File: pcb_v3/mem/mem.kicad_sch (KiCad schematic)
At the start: 27 parts, among them J1 bus mem, J2 bus mem, J3 cartridge, U1 CY62256-70PC, U2 CY62256-70PC, U3 74LS283, U4 74LS00, U5 74LS32, U7 74LS138

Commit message: avançando no layot v3
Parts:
- added J4: addr in, edge_connector:conector 02x08, symbol Connector_Generic:Conn_02x08_Odd_Even
- added RN1, RN2: 10K, Resistor_THT:R_Array_SIP9, symbol Device:R_Network08
- J1, J2: footprint Connector_PinHeader_2.54mm:PinHeader_2x08_P2.54mm_Vertical -> edge_connector:conector 02x08
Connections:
- net +5V: now also RN1.1 (common), RN2.1 (common)
- net addr_{0}: now also J4.2 (Pin_2), RN1.9 (R8)
- net addr_{10}: now also J4.12 (Pin_12), RN2.7 (R6)
- net addr_{11}: now also J4.11 (Pin_11), RN2.6 (R5)
- net addr_{12}: now also J4.14 (Pin_14), RN2.5 (R4)
- net addr_{13}: now also J4.13 (Pin_13), RN2.4 (R3)
- net addr_{14}: now also J4.16 (Pin_16), RN2.3 (R2)
- net addr_{15}: now also J4.15 (Pin_15), RN2.2 (R1)
- net addr_{1}: now also J4.1 (Pin_1), RN1.8 (R7)
- net addr_{2}: now also J4.4 (Pin_4), RN1.7 (R6)
- net addr_{3}: now also J4.3 (Pin_3), RN1.6 (R5)
- net addr_{4}: now also J4.6 (Pin_6), RN1.5 (R4)
- net addr_{5}: now also J4.5 (Pin_5), RN1.4 (R3)
- net addr_{6}: now also J4.8 (Pin_8), RN1.3 (R2)
- net addr_{7}: now also J4.7 (Pin_7), RN1.2 (R1)
- net addr_{8}: now also J4.10 (Pin_10), RN2.9 (R8)
- net addr_{9}: now also J4.9 (Pin_9), RN2.8 (R7)
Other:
- moved on the sheet: J2

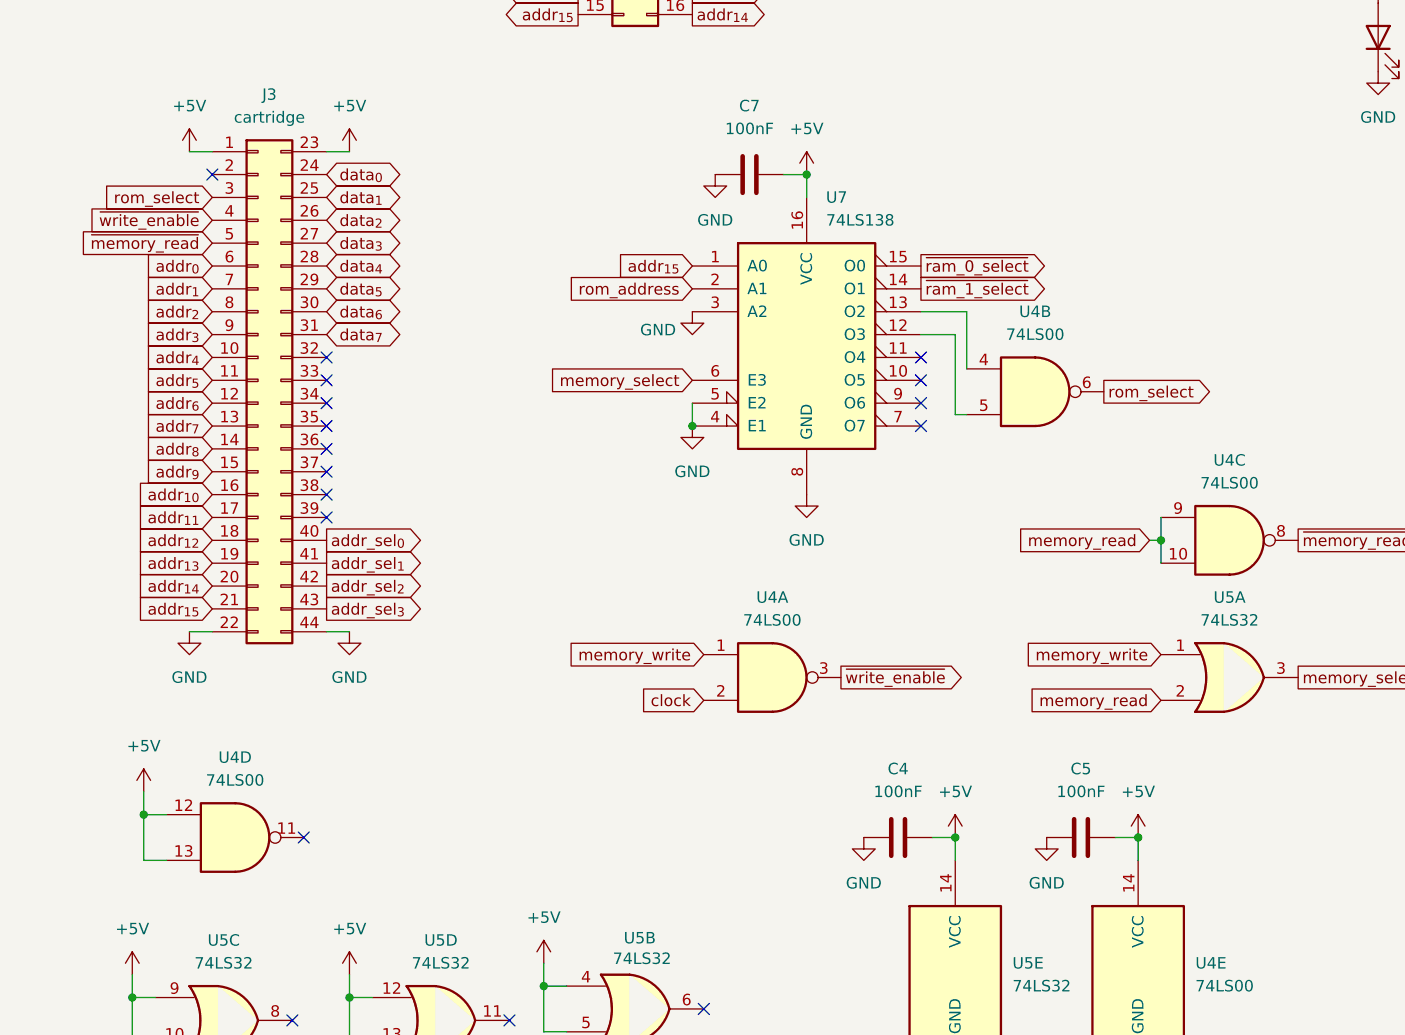
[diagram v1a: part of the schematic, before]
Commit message: seleção de chip de rom feita pela placa de memória; isso reduz um chip no cartucho
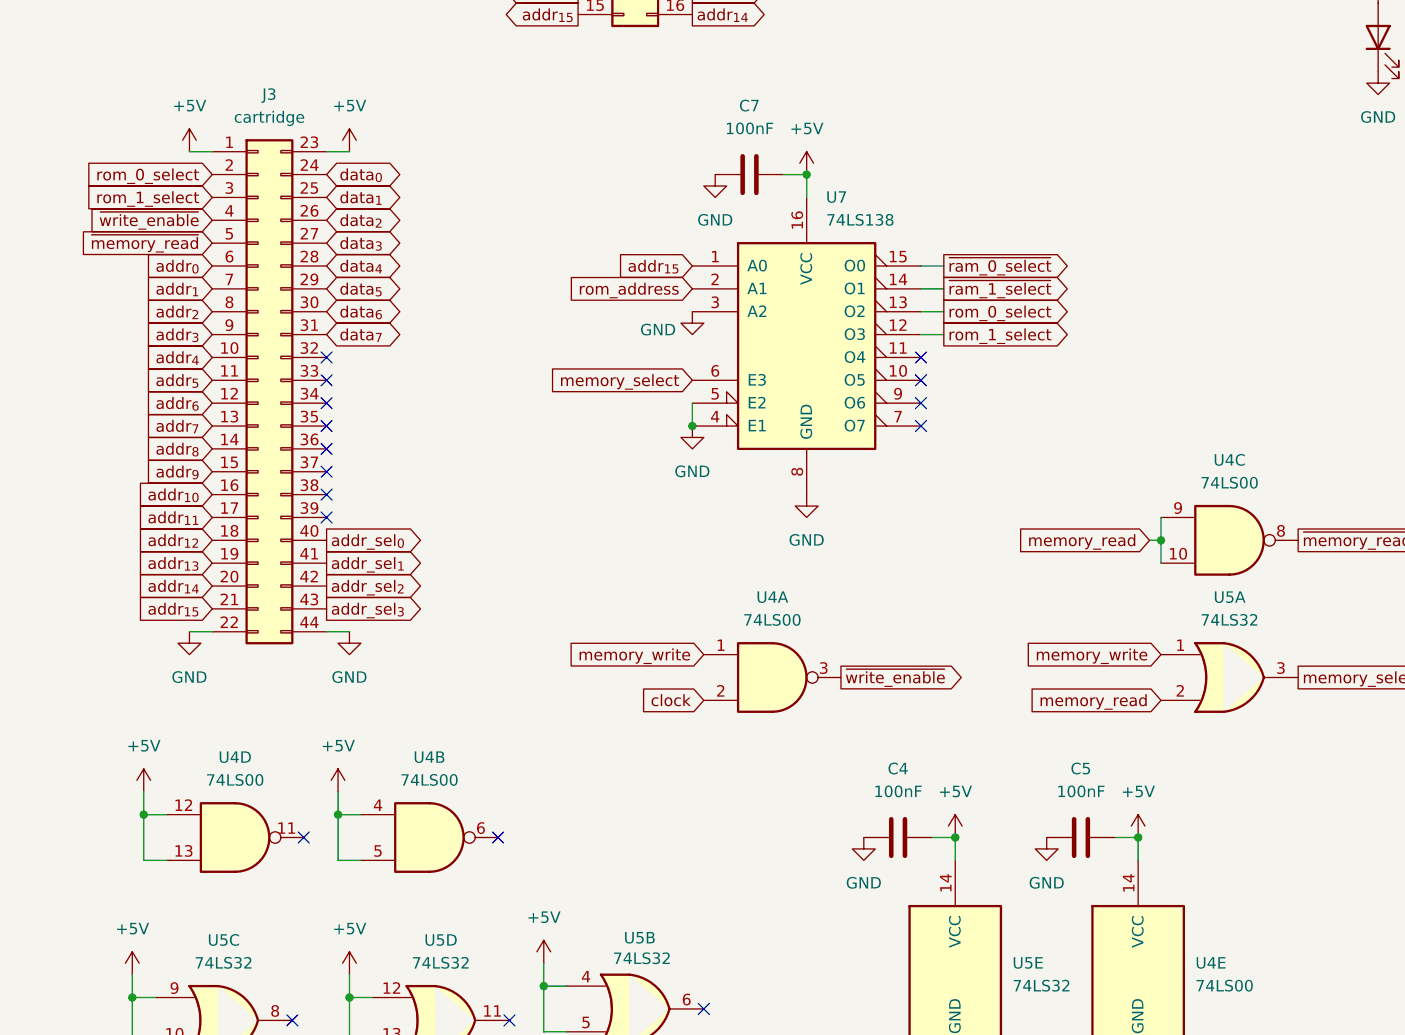
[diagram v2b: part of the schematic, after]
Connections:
- net +5V: now also U4.4, U4.5
- net rom_select: no longer J3.3 (Pin_3), U4.6
- net rom_0_select: now reaches U7.13 (O2)
- net rom_0_select: now also J3.2 (Pin_2); no longer U4.4
- net rom_1_select: now reaches U7.12 (O3)
- net rom_1_select: now also J3.3 (Pin_3); no longer U4.5
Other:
- moved on the sheet: U4B
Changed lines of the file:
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@@
 	)
 	(junction
+		(at 44.45 156.21)
+		(diameter 0)
+		(color 0 0 0 0)
+	)
+	(junction
 		(at 21.59 176.53)
 		(diameter 0)
@@
 	)
 	(no_connect
-		(at 30.48 85.09)
+		(at 41.91 45.72)
 	)
 	(no_connect
-		(at 41.91 45.72)
+		(at 62.23 158.75)
 	)
 	(no_connect
@@
 	(wire
 		(pts
-			(xy 114.3 106.68) (xy 114.3 100.33)
+			(xy 67.31 175.26) (xy 67.31 172.72)
 		)
 		(stroke
@@
 	(wire
 		(pts
-			(xy 67.31 175.26) (xy 67.31 172.72)
+			(xy 45.72 176.53) (xy 45.72 173.99)
 		)
 		(stroke
@@
 	(wire
 		(pts
-			(xy 45.72 176.53) (xy 45.72 173.99)
+			(xy 222.25 148.59) (xy 234.95 148.59)
 		)
 		(stroke
@@
 	(wire
 		(pts
-			(xy 222.25 148.59) (xy 234.95 148.59)
+			(xy 247.65 100.33) (xy 250.19 100.33)
 		)
 		(stroke
@@
 	(wire
 		(pts
-			(xy 247.65 100.33) (xy 250.19 100.33)
+			(xy 24.13 181.61) (xy 21.59 181.61)
 		)
 		(stroke
@@
 	(wire
 		(pts
-			(xy 24.13 181.61) (xy 21.59 181.61)
+			(xy 25.4 161.29) (xy 22.86 161.29)
 		)
 		(stroke
@@
 	(wire
 		(pts
-			(xy 25.4 161.29) (xy 22.86 161.29)
+			(xy 133.35 158.75) (xy 133.35 161.29)
 		)
 		(stroke
@@
 	(wire
 		(pts
-			(xy 133.35 158.75) (xy 133.35 161.29)
+			(xy 44.45 156.21) (xy 44.45 153.67)
 		)
 		(stroke
@@
 	(wire
 		(pts
+			(xy 44.45 156.21) (xy 46.99 156.21)
+		)
+		(stroke
+			(width 0)
+			(type default)
+		)
+	)
+	(wire
+		(pts
 			(xy 41.91 50.8) (xy 41.91 53.34)
 		)
@@
 	(wire
 		(pts
-			(xy 113.03 102.87) (xy 109.22 102.87)
+			(xy 111.76 102.87) (xy 109.22 102.87)
 		)
 		(stroke
@@
 	(wire
 		(pts
+			(xy 111.76 97.79) (xy 109.22 97.79)
+		)
+		(stroke
+			(width 0)
+			(type default)
+		)
+	)
+	(wire
+		(pts
 			(xy 48.26 181.61) (xy 45.72 181.61)
 		)
@@
 	(wire
 		(pts
-			(xy 114.3 111.76) (xy 113.03 111.76)
+			(xy 46.99 161.29) (xy 44.45 161.29)
 		)
 		(stroke
@@
 	(wire
 		(pts
-			(xy 114.3 100.33) (xy 109.22 100.33)
+			(xy 111.76 100.33) (xy 109.22 100.33)
 		)
 		(stroke
@@
 	(wire
 		(pts
-			(xy 113.03 111.76) (xy 113.03 102.87)
+			(xy 111.76 95.25) (xy 109.22 95.25)
+		)
+		(stroke
+			(width 0)
+			(type default)
+		)
+	)
+	(wire
+		(pts
+			(xy 44.45 161.29) (xy 44.45 156.21)
 		)
 		(stroke
@@
 		)
 	)
+	(global_label "rom_0_select"
+		(shape input)
+		(at 30.48 85.09 180)
+		(fields_autoplaced yes)
+		(effects
+			(font
+				(size 1.27 1.27)
+			)
+			(justify right)
+		)
+		(property "Intersheetrefs" "${INTERSHEET_REFS}"
+			(at 15.0368 85.09 0)
+			(effects
+				(font
+					(size 1.27 1.27)
+				)
+				(justify right)
+				(hide yes)
+			)
+		)
+	)
 	(global_label "data_{2}"
 		(shape bidirectional)
@@
 		)
 	)
+	(global_label "rom_1_select"
+		(shape output)
+		(at 111.76 102.87 0)
+		(fields_autoplaced yes)
+		(effects
+			(font
+				(size 1.27 1.27)
+			)
+			(justify left)
+		)
+		(property "Intersheetrefs" "${INTERSHEET_REFS}"
+			(at 127.2032 102.87 0)
+			(effects
+				(font
+					(size 1.27 1.27)
+				)
+				(justify left)
+				(hide yes)
+			)
+		)
+	)
 	(global_label "~{memory_read}"
 		(shape input)
@@
 	(global_label "~{ram_0_select}"
 		(shape output)
-		(at 109.22 95.25 0)
+		(at 111.76 95.25 0)
 		(fields_autoplaced yes)
 		(effects
@@
 		)
 		(property "Intersheetrefs" "${INTERSHEET_REFS}"
-			(at 124.6632 95.25 0)
+			(at 127.2032 95.25 0)
 			(effects
 				(font
@@
 		)
 	)
+	(global_label "rom_1_select"
+		(shape input)
+		(at 30.48 87.63 180)
+		(fields_autoplaced yes)
+		(effects
+			(font
+				(size 1.27 1.27)
+			)
+			(justify right)
+		)
+		(property "Intersheetrefs" "${INTERSHEET_REFS}"
+			(at 15.0368 87.63 0)
+			(effects
+				(font
+					(size 1.27 1.27)
+				)
+				(justify right)
+				(hide yes)
+			)
+		)
+	)
 	(global_label "addr_{5}"
 		(shape input)
@@
 		)
 	)
-	(global_label "rom_select"
-		(shape output)
-		(at 129.54 109.22 0)
-		(fields_autoplaced yes)
-		(effects
-			(font
-				(size 1.27 1.27)
-			)
-			(justify left)
-		)
-		(property "Intersheetrefs" "${INTERSHEET_REFS}"
-			(at 142.8061 109.22 0)
-			(effects
-				(font
-					(size 1.27 1.27)
-				)
-				(justify left)
-				(hide yes)
-			)
-		)
-	)
 	(global_label "data_{7}"
 		(shape bidirectional)
@@
 	(global_label "~{ram_1_select}"
 		(shape output)
-		(at 109.22 97.79 0)
+		(at 111.76 97.79 0)
 		(fields_autoplaced yes)
 		(effects
@@
 		)
 		(property "Intersheetrefs" "${INTERSHEET_REFS}"
-			(at 124.6632 97.79 0)
+			(at 127.2032 97.79 0)
 			(effects
 				(font
@@
 		)
 	)
-	(global_label "rom_select"
-		(shape input)
-		(at 30.48 87.63 180)
-		(fields_autoplaced yes)
-		(effects
-			(font
-				(size 1.27 1.27)
-			)
-			(justify right)
-		)
-		(property "Intersheetrefs" "${INTERSHEET_REFS}"
-			(at 17.2139 87.63 0)
-			(effects
-				(font
-					(size 1.27 1.27)
-				)
-				(justify right)
-				(hide yes)
-			)
-		)
-	)
 	(global_label "addr_{13}"
 		(shape output)
@@
 		)
 	)
+	(global_label "rom_0_select"
+		(shape output)
+		(at 111.76 100.33 0)
+		(fields_autoplaced yes)
+		(effects
+			(font
+				(size 1.27 1.27)
+			)
+			(justify left)
+		)
+		(property "Intersheetrefs" "${INTERSHEET_REFS}"
+			(at 127.2032 100.33 0)
+			(effects
+				(font
+					(size 1.27 1.27)
+				)
+				(justify left)
+				(hide yes)
+			)
+		)
+	)
 	(symbol
 		(lib_id "power:GND")
@@
 	(symbol
 		(lib_id "74xx:74LS00")
-		(at 121.92 109.22 0)
+		(at 54.61 158.75 0)
 		(unit 2)
 		(exclude_from_sim no)
@@
 		(fields_autoplaced yes)
 		(property "Reference" "U4"
-			(at 121.9117 100.33 0)
+			(at 54.6017 149.86 0)
 			(effects
 				(font
@@
 		)
 		(property "Value" "74LS00"
-			(at 121.9117 102.87 0)
+			(at 54.6017 152.4 0)
 			(effects
 				(font
@@
 		)
 		(property "Footprint" "Package_DIP:DIP-14_W7.62mm"
-			(at 121.92 109.22 0)
+			(at 54.61 158.75 0)
 			(effects
 				(font
@@
 		)
 		(property "Datasheet" "http://www.ti.com/lit/gpn/sn74ls00"
-			(at 121.92 109.22 0)
+			(at 54.61 158.75 0)
 			(effects
 				(font
@@
 		)
 		(property "Description" "quad 2-input NAND gate"
-			(at 121.92 109.22 0)
+			(at 54.61 158.75 0)
 			(effects
 				(font
@@
 					(unit 1)
 				)
+			)
+		)
+	)
+	(symbol
+		(lib_id "power:+5V")
+		(at 44.45 153.67 0)
+		(unit 1)
+		(exclude_from_sim no)
+		(in_bom yes)
+		(on_board yes)
+		(dnp no)
+		(fields_autoplaced yes)
+		(property "Reference" "#PWR036"
+			(at 44.45 157.48 0)
+			(effects
+				(font
+					(size 1.27 1.27)
+				)
+				(hide yes)
+			)
+		)
+		(property "Value" "+5V"
+			(at 44.45 148.59 0)
+			(effects
+				(font
+					(size 1.27 1.27)
+				)
+			)
+		)
+		(property "Footprint" ""
+			(at 44.45 153.67 0)
+			(effects
+				(font
+					(size 1.27 1.27)
+				)
+				(hide yes)
+			)
+		)
+		(property "Datasheet" ""
+			(at 44.45 153.67 0)
+			(effects
+				(font
+					(size 1.27 1.27)
+				)
+				(hide yes)
+			)
+		)
+		(property "Description" "Power symbol creates a global label with name \"+5V\""
+			(at 44.45 153.67 0)
+			(effects
+				(font
+					(size 1.27 1.27)
+				)
+				(hide yes)
+			)
+		)
+		(pin "1"
+		)
+		(instances
+			(project "mem"
+				(path "/98924365-9bd1-4f01-bbcb-a70fa683291e"
+					(reference "#PWR036")
+					(unit 1)
+				)
